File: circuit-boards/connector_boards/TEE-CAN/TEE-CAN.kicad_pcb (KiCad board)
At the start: 2 copper layers, 19.1 x 50.8 mm, 8 parts, among them J1 Conn_01x02_Pin, J2 Conn_01x02_Pin, J3 Conn_01x02_Pin, J4 Conn_01x02_Pin

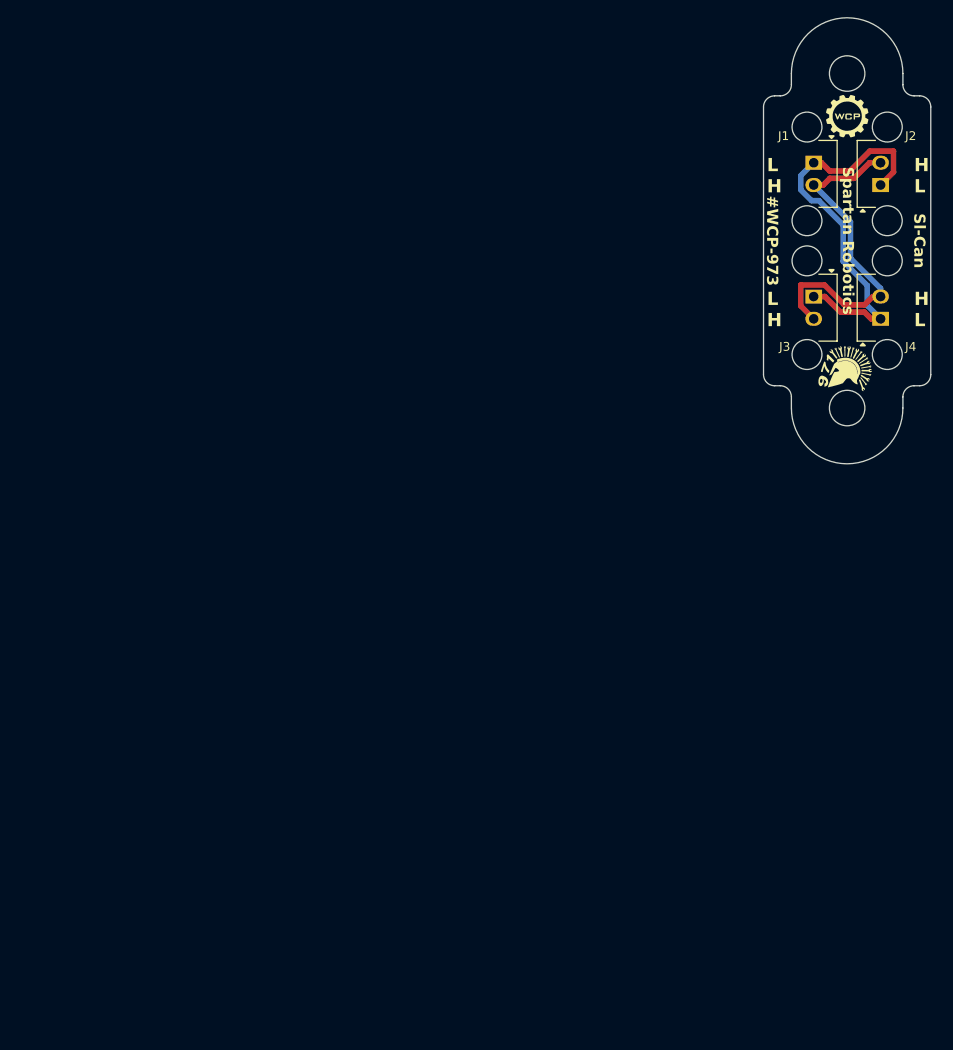
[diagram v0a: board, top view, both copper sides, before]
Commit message: Export files for new pcbs + board characteristics
Signed-off-by: Alex lenkov <Alexander.i.lenkov@gmail.com>
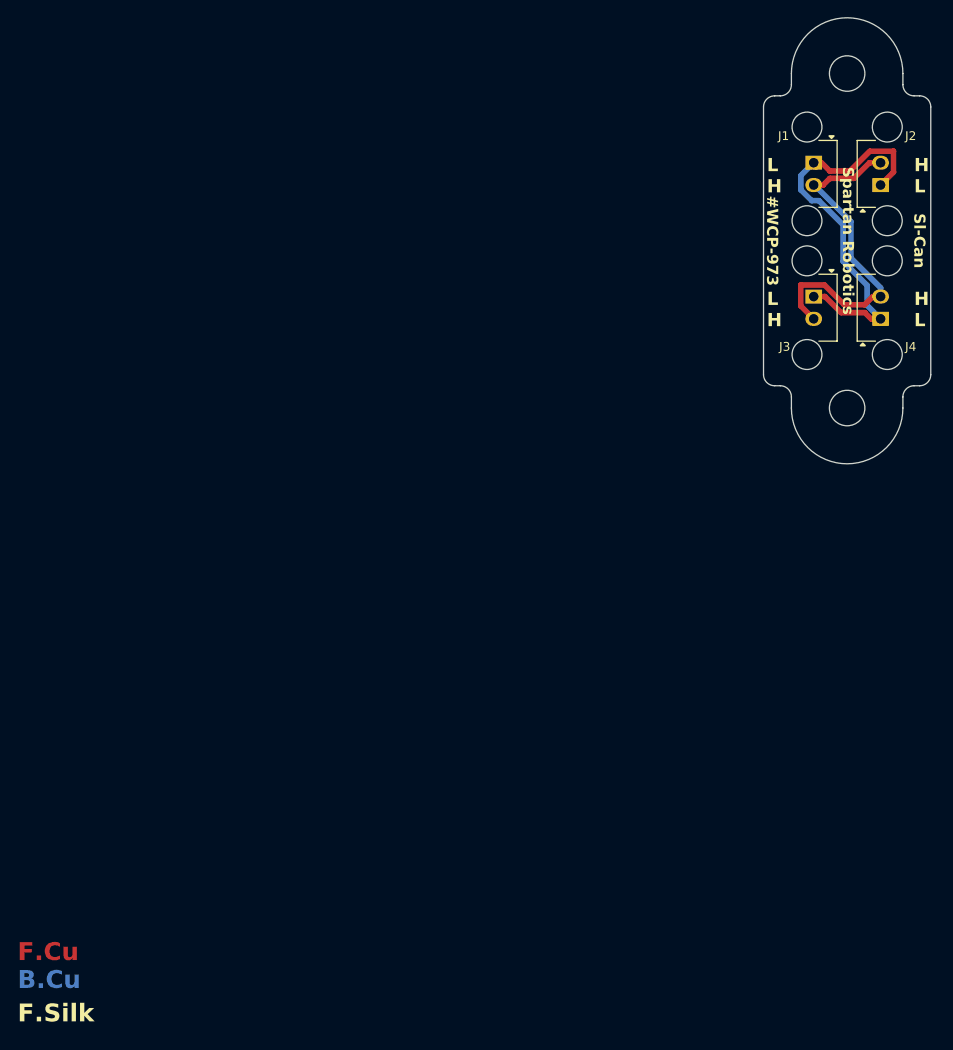
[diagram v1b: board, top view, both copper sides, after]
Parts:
- G*** (x2): moved to B.Cu
- turned G*** to 180 degrees
- turned G*** to -170 degrees
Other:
- board text added: "0"
- board text added: "0 mm"
- board text added: "0.0000 mm / 0.2540 mm"
- board text added: "0.01 mm"
- board text added: "0.02"
- board text added: "0.035 mm"
- board text added: "0.3000 mm"
- board text added: "1"
- board text added: "1 oz"
- board text added: "1.51 mm"
- board text added: "1.6000 mm"
- board text added: "1.Layers: 2 2.Thickness: 1.6 3.Surface finish: HASL 4.Outer Copper Weight: 1oz 5.Via covering: Tented 6.Min hole size: .3mm 7.Gold Fingers: No 8.Castellated Holes: No 9.Edge Plating: No"
- board text added: "19.0500 mm x 50.7951 mm"
- board text added: "2"
- board text added: "3.3"
- board text added: "4.5"
- board text added: "B.Cu"
- board text added: "B.Mask"
- board text added: "B.Paste"
- board text added: "B.Silk"
- board text added: "B.Silkscreen"
- board text added: "BOARD CHARACTERISTICS"
- board text added: "Board Thickness:"
- board text added: "Board overall dimensions:"
- board text added: "Bottom Silk Screen"
- board text added: "Bottom Solder Mask"
- board text added: "Bottom Solder Paste"
- board text added: "Castellated pads:"
- board text added: "Color"
- board text added: "Copper Finish:"
- board text added: "Copper Layer Count:"
- board text added: "Dielectric"
- board text added: "Edge card connectors:"
- board text added: "Edge.Cuts"
- board text added: "Epsilon R"
- board text added: "F.Cu"
- board text added: "F.Mask"
- board text added: "F.Paste"
- board text added: "F.Silk"
- board text added: "F.Silkscreen"
- board text added: "FR4"
- board text added: "HASL"
- board text added: "Impedance Control:"
- board text added: "LAYERS"
- board text added: "Layer Name"
- board text added: "Loss Tangent"
- board text added: "Margin"
- board text added: "Material"
- board text added: "Min hole diameter:"
- board text added: "Min track/spacing:"
- board text added: "NOTES"
- board text added: "No"
- board text added: "Not specified"
- board text added: "Outer Copper Weight:"
- board text added: "Plated Board Edge:"
- board text added: "Tented"
- board text added: "Thickness (mm)"
- board text added: "Top Silk Screen"
- board text added: "Top Solder Mask"
- board text added: "Top Solder Paste"
- board text added: "Type"
- board text added: "User.1"
- board text added: "Via type:"
- board text added: "copper"
- board text added: "core"
